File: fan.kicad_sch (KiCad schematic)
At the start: 14 parts, among them J7 Conn_01x04, J8 Conn_01x04, U13 EMC2302

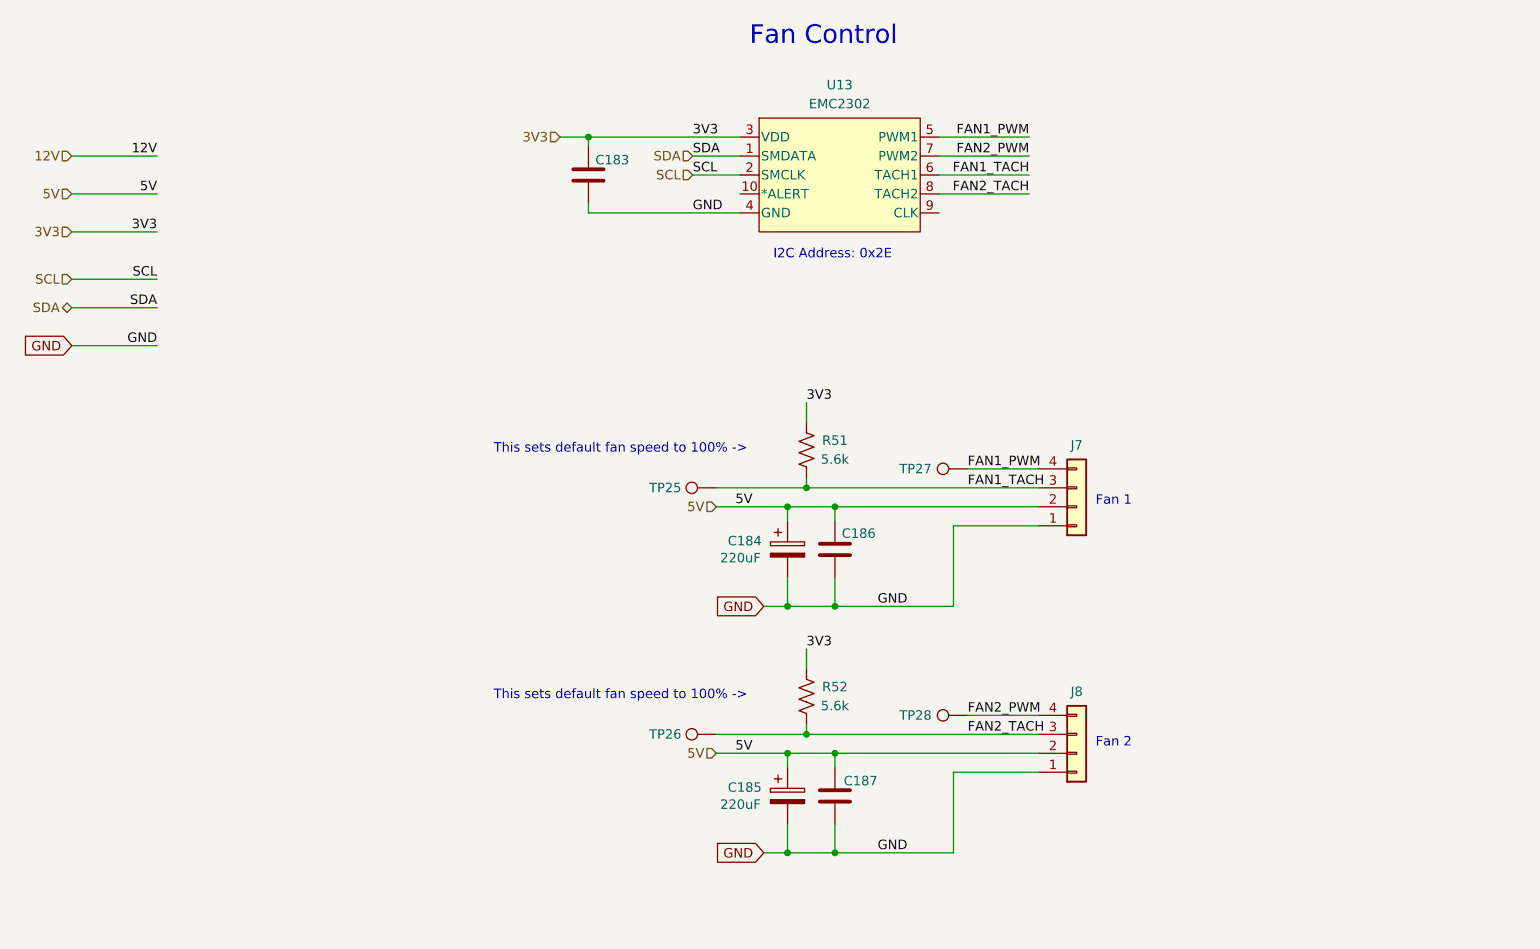
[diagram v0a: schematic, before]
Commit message: ASICs placed. most other parts placed.
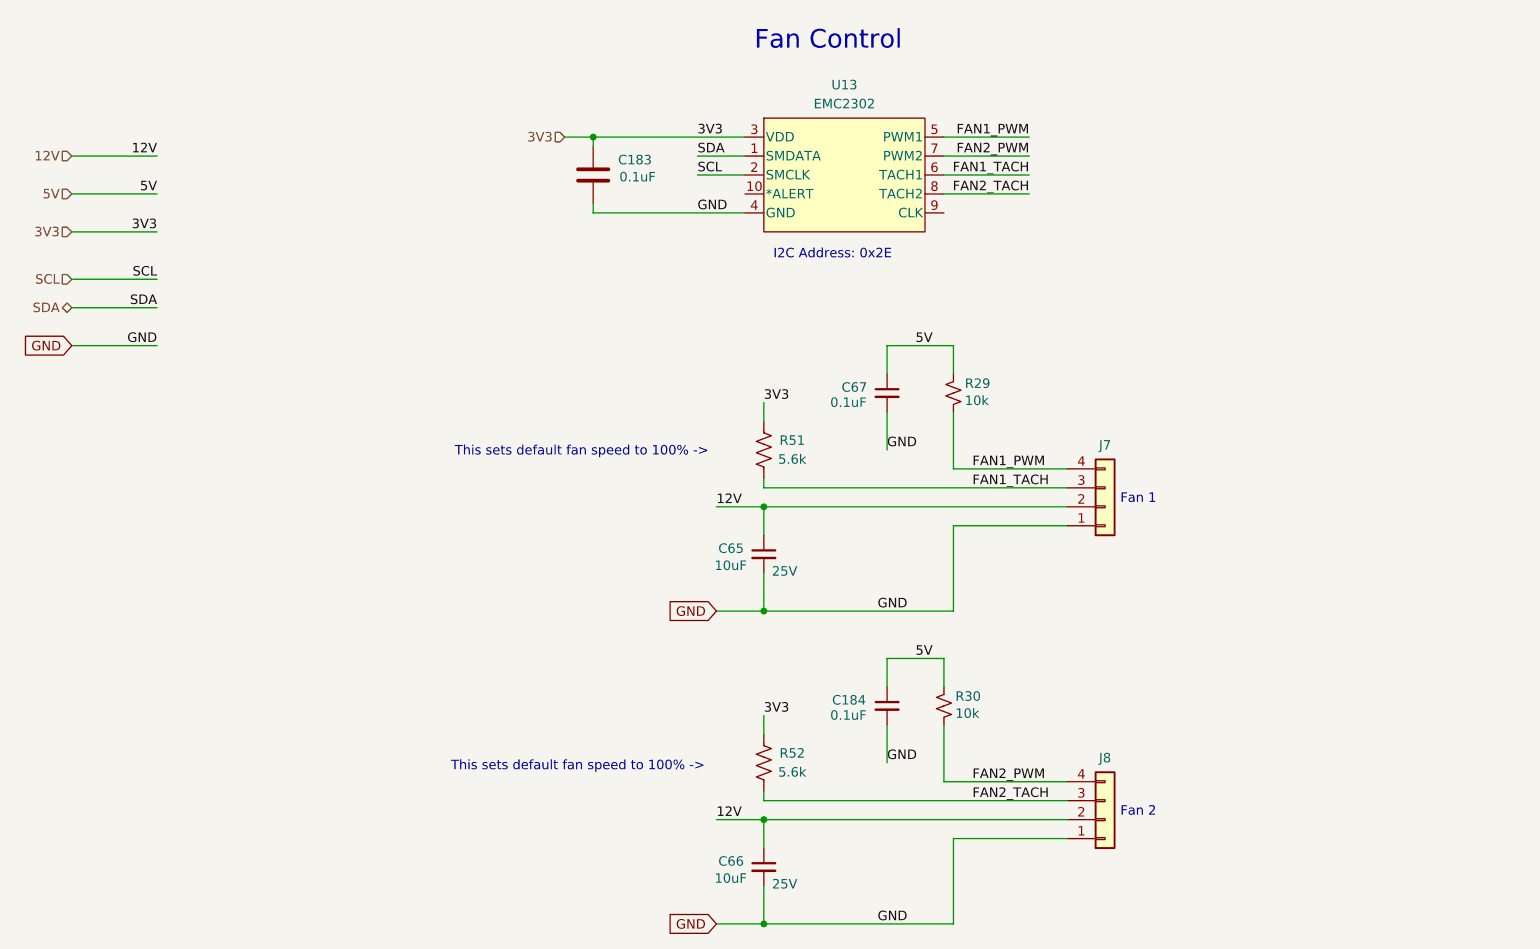
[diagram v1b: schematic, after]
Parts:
- removed C184, C185: 220uF, Capacitor_SMD:CP_Elec_6.3x7.7, symbol Device:C_Polarized
- removed C186, C187: 311-3342-1-ND, Capacitor_SMD:C_0402_1005Metric, symbol Device:C
- removed TP25, TP26, TP27, TP28: TestPoint, TestPoint:TestPoint_Pad_D1.0mm, symbol Connector:TestPoint
- added C184, C67: 0.1uF, Capacitor_SMD:C_0402_1005Metric, symbol Device:C_Small
- added C65, C66: 10uF, Capacitor_SMD:C_0603_1608Metric, symbol Device:C_Small
- added R29, R30: 10k, Resistor_SMD:R_0402_1005Metric, symbol Device:R_Small_US
- C183: value 311-3342-1-ND -> 0.1uF
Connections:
- net 12V: now also J7.2 (Pin_2), J8.2 (Pin_2), C65.1, C66.1
- net 5V: now also C184.1, C67.1, R29.2, R30.2; no longer J7.2 (Pin_2), J8.2 (Pin_2)
- net FAN1_PWM: now also R29.1
- net FAN2_PWM: now also R30.1
- net GND: now also C184.2, C65.2, C66.2, C67.2
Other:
- moved on the sheet: C183, J7, J8, R51, R52, U13

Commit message: switch to the bitaxeBIRDS based pre-bonanza
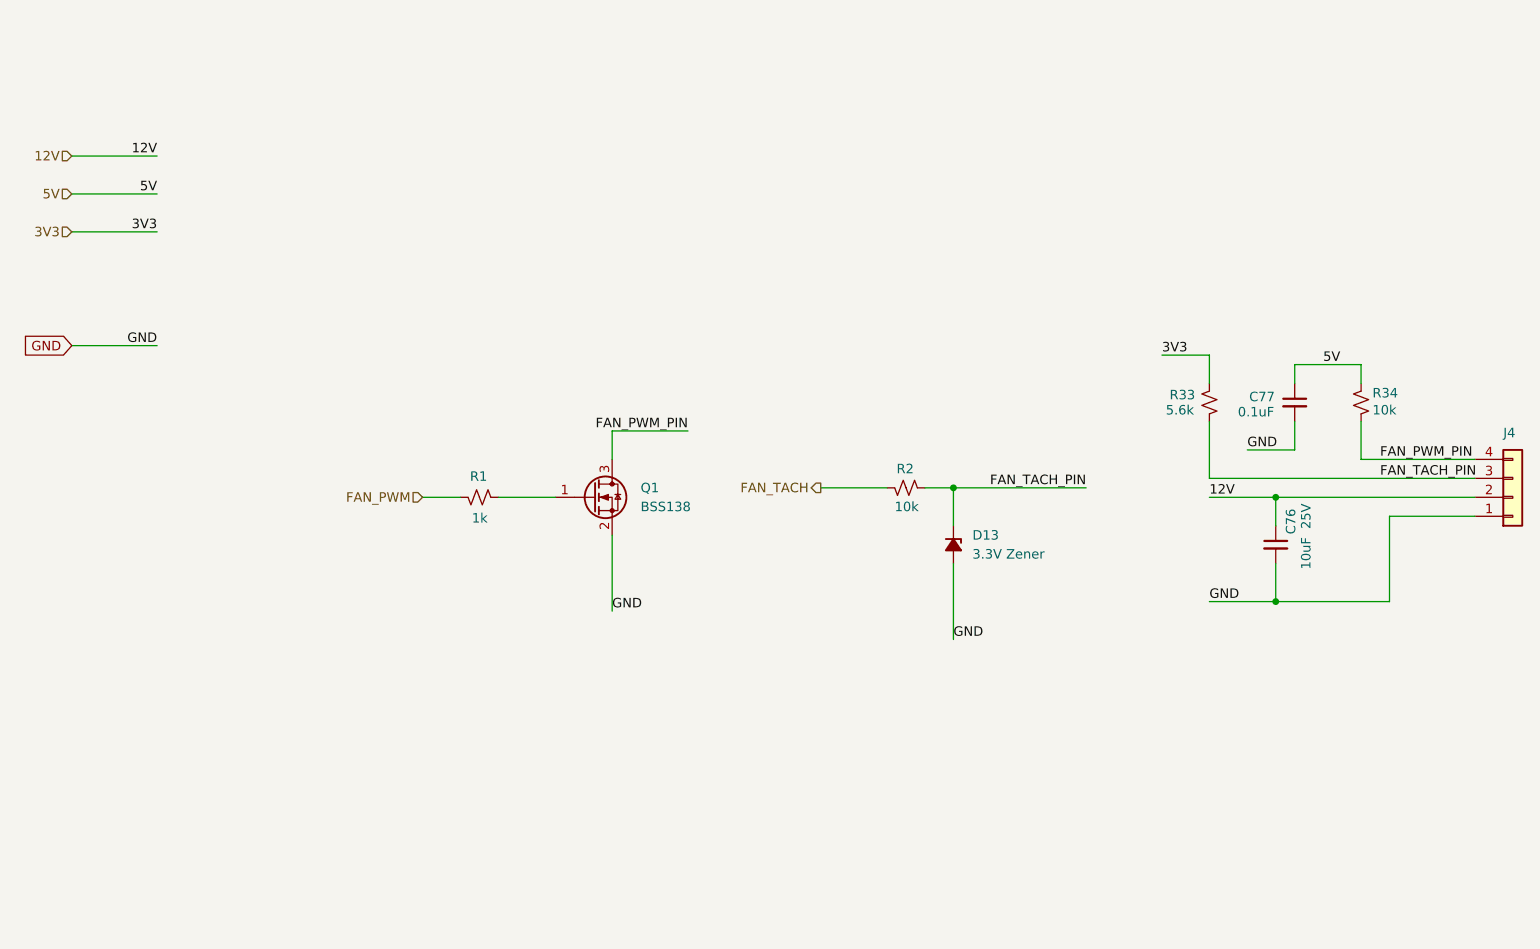
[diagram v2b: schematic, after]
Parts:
- removed C183: 0.1uF, Capacitor_SMD:C_0402_1005Metric, symbol Device:C
- removed C184: 0.1uF, Capacitor_SMD:C_0402_1005Metric, symbol Device:C_Small
- removed C66: 10uF, Capacitor_SMD:C_0603_1608Metric, symbol Device:C_Small
- removed J7, J8: Conn_01x04, bitaxe:470531000, symbol Connector_Generic:Conn_01x04
- removed R30: 10k, Resistor_SMD:R_0402_1005Metric, symbol Device:R_Small_US
- removed R51, R52: 5.6k, Resistor_SMD:R_0402_1005Metric, symbol Device:R_US
- removed U13: EMC2302, Package_SO:MSOP-10_3x3mm_P0.5mm, symbol bitaxe:EMC2302-2-AIZL-TR
- added D13: 3.3V Zener, Diode_SMD:D_SOD-123, symbol Device:D_Zener_Small_Filled
- added J4: Conn_01x04, bitaxe:470531000, symbol Connector_Generic:Conn_01x04
- added Q1: BSS138, Package_TO_SOT_SMD:SOT-23, symbol Transistor_FET:BSS138
- added R1: 1k, Resistor_SMD:R_0402_1005Metric, symbol Device:R_Small_US
- added R2: 10k, Resistor_SMD:R_0402_1005Metric, symbol Device:R_Small_US
- added R33: 5.6k, Resistor_SMD:R_0402_1005Metric, symbol Device:R_Small_US
- renumbered C65 to C76, C67 to C77, R29 to R34
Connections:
- net 12V: now also J4.2 (Pin_2)
- net 3V3: now also R33.2
- net GND: now also D13.2 (A), J4.1 (Pin_1), Q1.2 (S)
- net FAN1_PWM renamed FAN_PWM_PIN
- net FAN_PWM_PIN: now also J4.4 (Pin_4), Q1.3 (D)
- new net: Q1.1 (G), R1.1
- new net FAN_PWM: R1.2
- new net FAN_TACH: R2.2
- new net FAN_TACH_PIN: D13.1 (K), J4.3 (Pin_3), R2.1, R33.1
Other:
- note removed: "Fan 1"
- note removed: "Fan 2"
- note removed: "Fan Control"
- note removed: "I2C Address: 0x2E"
- note removed: "This sets default fan speed to 100% ->"
- moved on the sheet: C76, C77, R34

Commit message: updated schematic worksheet
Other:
- company: (none) -> bitaxeorg
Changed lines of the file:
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@@
 		(date "2026-02-11")
 		(rev "1002x")
+		(company "bitaxeorg")
+		(comment 1 "OHL v2")
 	)
 	(junction

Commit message: switched back to TPS82130. added BOM partnumbers
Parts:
- C77: LCSC (none) -> C307331
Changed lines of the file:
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@@
+			)
+		)
+		(property "Height" ""
+			(at 127 92.71 0)
+			(effects
+				(font
+					(size 1.27 1.27)
+				)
+				(hide yes)
 			)
 		)
@@
 			)
 		)
+		(property "Height" ""
+			(at 168.91 91.44 90)
+			(effects
+				(font
+					(size 1.27 1.27)
+				)
+				(hide yes)
+			)
+		)
 		(pin "2"
 		)
@@
 			)
 		)
+		(property "Height" ""
+			(at 229.87 80.01 0)
+			(effects
+				(font
+					(size 1.27 1.27)
+				)
+				(hide yes)
+			)
+		)
 		(pin "2"
 		)
@@
 			)
 		)
+		(property "Height" ""
+			(at 175.26 99.06 90)
+			(effects
+				(font
+					(size 1.27 1.27)
+				)
+				(hide yes)
+			)
+		)
 		(pin "1"
 		)
@@
 			)
 		)
+		(property "Height" ""
+			(at 250.19 92.71 0)
+			(effects
+				(font
+					(size 1.27 1.27)
+				)
+				(hide yes)
+			)
+		)
 		(pin "4"
 		)
@@
 			)
 		)
+		(property "Height" ""
+			(at 209.55 80.01 0)
+			(effects
+				(font
+					(size 1.27 1.27)
+				)
+				(hide yes)
+			)
+		)
 		(pin "2"
 		)
@@
 			)
 		)
+		(property "Height" ""
+			(at 111.76 92.71 90)
+			(effects
+				(font
+					(size 1.27 1.27)
+				)
+				(hide yes)
+			)
+		)
 		(pin "2"
 		)
@@
 			)
 		)
+		(property "Height" ""
+			(at 220.98 80.01 0)
+			(effects
+				(font
+					(size 1.27 1.27)
+				)
+				(hide yes)
+			)
+		)
+		(property "LCSC" "C307331"
+			(at 220.98 80.01 0)
+			(effects
+				(font
+					(size 1.27 1.27)
+				)
+				(hide yes)
+			)
+		)
 		(pin "1"
 		)
@@
 			(at 218.44 99.06 90)
 			(effects
+				(font
+					(size 1.27 1.27)
+				)
+				(hide yes)
+			)
+		)
+		(property "Height" ""
+			(at 218.44 99.06 90)
+			(effects
